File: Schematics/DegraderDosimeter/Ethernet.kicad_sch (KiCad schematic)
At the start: 38 parts, among them J1 RJ45_Amphenol_RJMG1BD3B8K1ANR, U1 LAN8742A, U2 USBLC6-4SC6, U3 H1102NL, Y1 Crystal

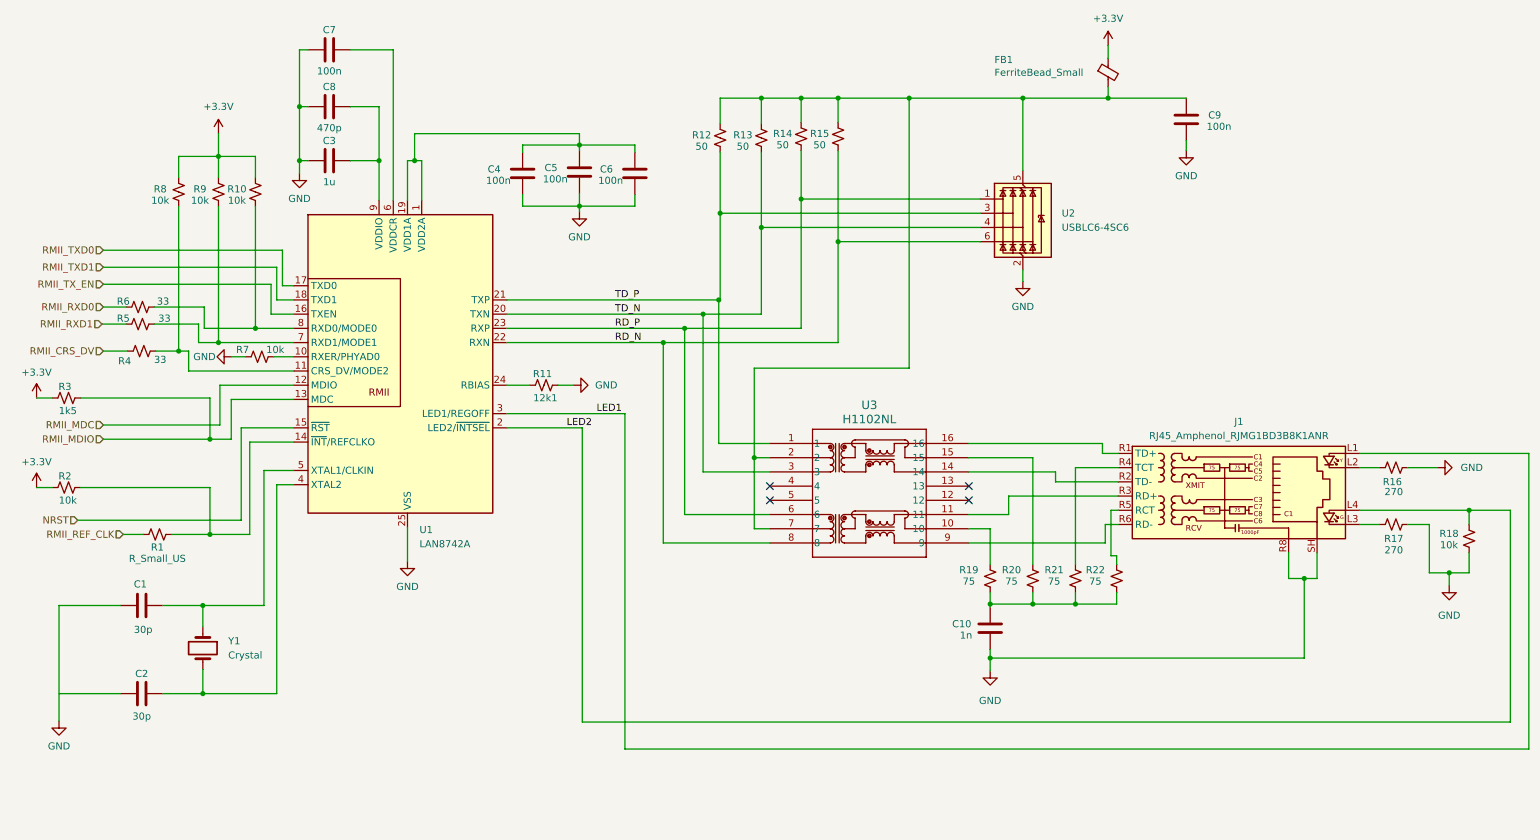
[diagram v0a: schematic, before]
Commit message: Bring the DegraderDosimeter schematic up to a routable state
Single ECAD commit on top of "First upload", carrying both the earlier
board-bring-up work and this session's changes. Squashed here so the
schematic history is separate from the FirmwareUpdate restructure, which
stays on main.

Library resolution
  Register the A4988 and LM60430DRPKR symbol libraries in sym-lib-table,
  and the DE15, DRIVER-A4988SETTR-T_QFN28_ and KRJ-CB4.2GYZNL footprint
  libraries in fp-lib-table. Point H1102NL at ${KIPRJMOD} instead of the
  undefined ${CUSTOM}. All 26 symbols and 24 footprints now resolve.

Degrader to MCU
  Wire all 32 degrader signals to the STM32H723: 11 A4988/L293D controls
  and 21 lens limit switches. Reuse the F746 firmware's pin assignment
  where it does not clash with the dosimeter; MS1 and MS2 move to PD14
  and PD15 because PD11/PD12 are pulse-capture pins, and !ENABLE takes
  PB7 as the firmware never assigned it. Grow the MCU_H723 sheet so its
  right edge spans the Degrader sheet, giving one straight wire per net.

Net naming and classes
  Drop the duplicate port label on the 50 pins that already carry a
  functional hierarchical label, so nets read STEP/MS1/RMII_REF_CLK
  rather than PD14/PA1; unused pins keep their port label and bus. Name
  the remaining 73 auto-named nets. Add ETH_DIFF_100R, ETH_RMII, POWER,
  MOTOR and ANALOG net classes. The four MDI pairs get 0.15 mm track on
  a 0.30 mm gap, which is 100 ohm differential on the declared stackup
  (F.Cu over In1.Cu, 0.1 mm prepreg, er 4.5) - reconfirm if the fab
  ships a different stackup.

Connection fixes
  - MDC/MDIO were crossed: PA2 landed on the PHY's MDC pin and PC1 on
    MDIO. Swapped the two labels in Ethernet.kicad_sch.
  - PULSE_6 moved PD11 -> PD12, the TIM4_CH1 pin BLM_Code.ioc expects.
  - PulseShaper 1, 2 and 5 outputs missed their sheet pins by 2-81 um.
  - XTAL1 stopped 0.254 mm short of Y1/C1, leaving the PHY crystal open.
  - C32/C35 and C39/C40, the U5 and U7 cap returns, h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
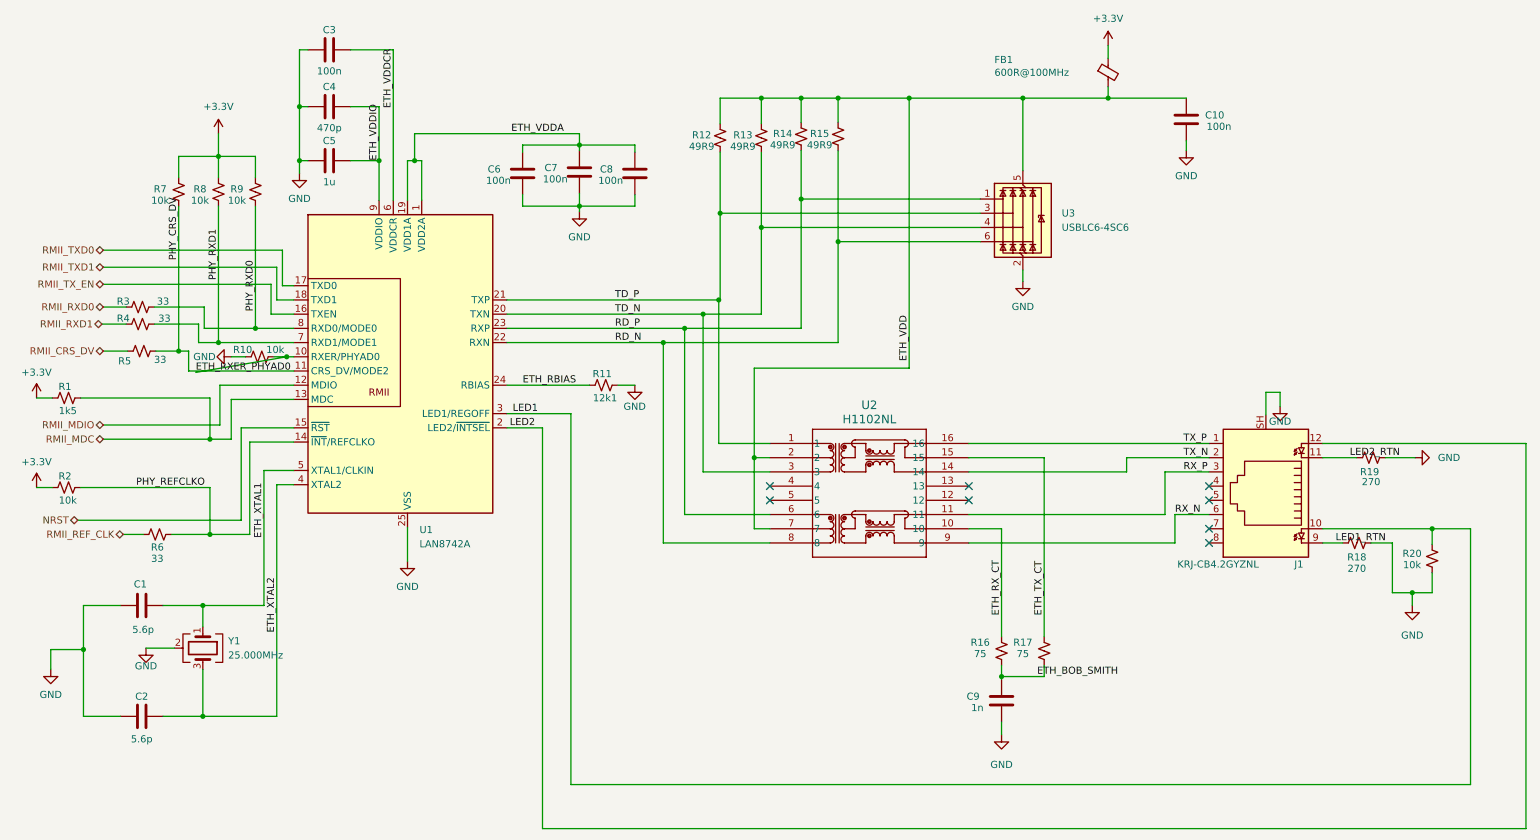
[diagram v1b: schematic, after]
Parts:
- removed J1: RJ45_Amphenol_RJMG1BD3B8K1ANR, Connector_RJ:RJ45_Pulse_JK0654219NL_Horizontal, symbol Connector:RJ45_Amphenol_RJMG1BD3B8K1ANR
- removed R21, R22: 75, Capacitor_SMD:C_1206_3216Metric, symbol Device:R_Small_US
- added J1: KRJ-CB4.2GYZNL, KRJ-CB4.2GYZNL:KRJ-CB4.2GYZNL, symbol Connector:RJ45_LED_Shielded
- C1, C2: value 30p -> 5.6p
- FB1: value FerriteBead_Small -> 600R@100MHz; footprint Ferrite_THT:LairdTech_28C0236-0JW-10 -> Inductor_SMD:L_0603_1608Metric
- R1: renamed from R3; footprint Capacitor_SMD:C_1206_3216Metric -> Resistor_SMD:R_1206_3216Metric_Pad1.30x1.75mm_HandSolder
- R10: renamed from R7; footprint Capacitor_SMD:C_1206_3216Metric -> Resistor_SMD:R_1206_3216Metric_Pad1.30x1.75mm_HandSolder
- R11, R2: footprint Capacitor_SMD:C_1206_3216Metric -> Resistor_SMD:R_1206_3216Metric_Pad1.30x1.75mm_HandSolder
- R12, R13, R14, R15: value 50 -> 49R9; footprint Capacitor_SMD:C_1206_3216Metric -> Resistor_SMD:R_1206_3216Metric_Pad1.30x1.75mm_HandSolder
- R16: renamed from R19; footprint Capacitor_SMD:C_1206_3216Metric -> Resistor_SMD:R_1206_3216Metric_Pad1.30x1.75mm_HandSolder
- R17: renamed from R20; footprint Capacitor_SMD:C_1206_3216Metric -> Resistor_SMD:R_1206_3216Metric_Pad1.30x1.75mm_HandSolder
- R18: renamed from R17; footprint Capacitor_SMD:C_1206_3216Metric -> Resistor_SMD:R_1206_3216Metric_Pad1.30x1.75mm_HandSolder
- R19: renamed from R16; footprint Capacitor_SMD:C_1206_3216Metric -> Resistor_SMD:R_1206_3216Metric_Pad1.30x1.75mm_HandSolder
- R20: renamed from R18; footprint Capacitor_SMD:C_1206_3216Metric -> Resistor_SMD:R_1206_3216Metric_Pad1.30x1.75mm_HandSolder
- R3: renamed from R6; footprint Capacitor_SMD:C_1206_3216Metric -> Resistor_SMD:R_1206_3216Metric_Pad1.30x1.75mm_HandSolder
- R4: renamed from R5; footprint Capacitor_SMD:C_1206_3216Metric -> Resistor_SMD:R_1206_3216Metric_Pad1.30x1.75mm_HandSolder
- R5: renamed from R4; footprint Capacitor_SMD:C_1206_3216Metric -> Resistor_SMD:R_1206_3216Metric_Pad1.30x1.75mm_HandSolder
- R6: renamed from R1; value R_Small_US -> 33; footprint Capacitor_SMD:C_1206_3216Metric -> Resistor_SMD:R_1206_3216Metric_Pad1.30x1.75mm_HandSolder
- R7: renamed from R8; footprint Capacitor_SMD:C_1206_3216Metric -> Resistor_SMD:R_1206_3216Metric_Pad1.30x1.75mm_HandSolder
- R8: renamed from R9; footprint Capacitor_SMD:C_1206_3216Metric -> Resistor_SMD:R_1206_3216Metric_Pad1.30x1.75mm_HandSolder
- R9: renamed from R10; footprint Capacitor_SMD:C_1206_3216Metric -> Resistor_SMD:R_1206_3216Metric_Pad1.30x1.75mm_HandSolder
- Y1: value Crystal -> 25.000MHz; footprint Crystal:Crystal_SMD_Abracon_ABM10-4Pin_2.5x2.0mm -> Crystal:Crystal_SMD_2016-4Pin_2.0x1.6mm; symbol Device:Crystal -> Device:Crystal_GND24
- renumbered C9 to C10, C7 to C3, C8 to C4, C3 to C5, C4 to C6, C5 to C7, C6 to C8, C10 to C9, U3 to U2, U2 to U3
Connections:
- net GND: now also C2.1, Y1.2 (G), Y1.4 (G), J1.SH
- net LED1: now also R20.2, J1.10
- net LED2: now also J1.12; no longer R20.2
- net RMII_MDC: now also R1.2, U1.13 (MDC); no longer U1.12 (MDIO)
- net RMII_MDIO: now also U1.12 (MDIO); no longer R1.2, U1.13 (MDC)
- net ETH_BOB_SMITH: now reaches C9.1, R16.2, R17.2
- net ETH_VDDA: now reaches C6.1, C7.1, C8.1, U1.1 (VDD2A), U1.19 (VDD1A)
- net ETH_RXER_PHYAD0: now reaches R10.2, U1.10 (RXER/PHYAD0)
- net PHY_CRS_DV: now reaches R5.2, R7.1, U1.11 (CRS_DV/MODE2)
- net PHY_REFCLKO: now reaches R2.2, R6.2, U1.14 (~{INT}/REFCLKO)
- net ETH_RBIAS: now reaches R11.1, U1.24 (RBIAS)
- net ETH_XTAL2: now reaches C2.2, U1.4 (XTAL2)
- net ETH_XTAL2: now also Y1.3; no longer Y1.2
- net ETH_XTAL1: now reaches C1.2, U1.5 (XTAL1/CLKIN), Y1.1
- net ETH_VDDCR: now reaches C3.1, U1.6 (VDDCR)
- net PHY_RXD1: now reaches R4.2, R8.1, U1.7 (RXD1/MODE1)
- net PHY_RXD0: now reaches R3.2, R9.1, U1.8 (RXD0/MODE0)
- net ETH_VDDIO: now reaches C4.1, C5.1, U1.9 (VDDIO)
- net ETH_TX_CT: now reaches R17.1, U2.15
- net ETH_VDD: now reaches C10.1, FB1.2, R12.2, R13.2, R14.2, R15.2, U2.2, U2.7, U3.5 (VBUS)
- net ETH_RX_CT: now reaches R16.1, U2.10
- net RX_P: now reaches U2.11
- net RX_P: now also J1.3
- net TX_N: now reaches U2.14
- net TX_N: now also J1.2
- net TX_P: now reaches U2.16
- net TX_P: now also J1.1
- net RX_N: now reaches U2.9
- net RX_N: now also J1.6
- net LED2_RTN: now reaches R19.1
- net LED2_RTN: now also J1.11
- net LED1_RTN: now reaches R18.2
- net LED1_RTN: now also J1.9
- no-connect marks 4 -> 8
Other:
- moved on the sheet: C2, C9, R11, R16, R17, R18, R19, R20
